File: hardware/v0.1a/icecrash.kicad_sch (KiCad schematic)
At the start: 62 parts, among them J1 SNES, J2 HDMI_A, J3 pkl_jumper, J5 Conn_02x08_Odd_Even, SW1 TACT, U1 74LVC2T45, U2 74LVC2T45, U3 74LVC2T45, U4 SII902xA-mod, U5 TLV62568DBV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

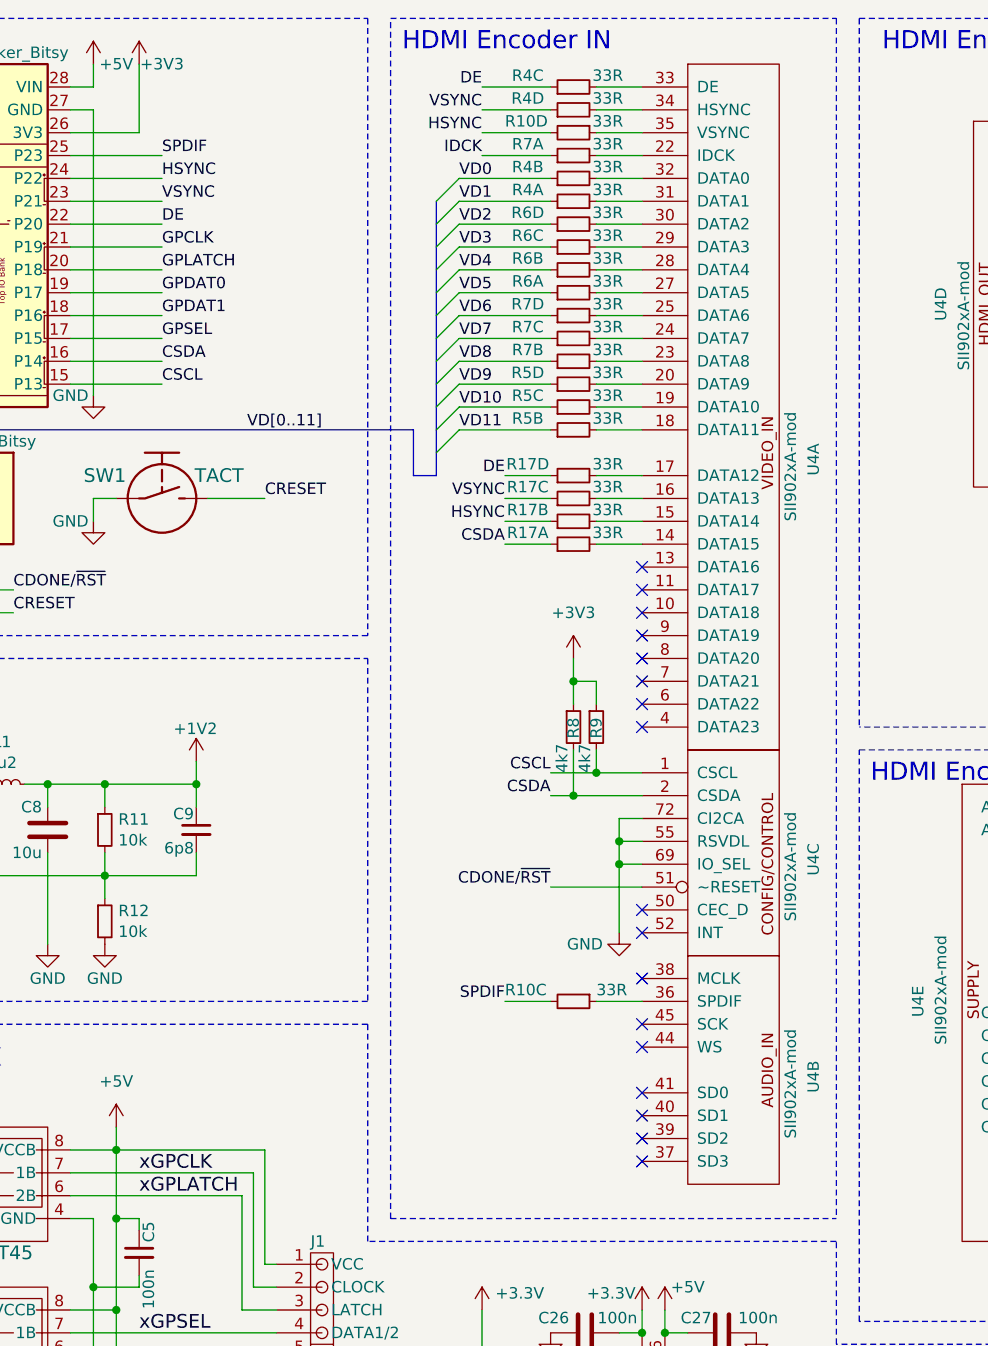
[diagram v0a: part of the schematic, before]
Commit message: Changed the HDMI encoder wiring a bit.
It is better to leave the sync signals alone. We can double assign some
of the data pins to gain access to a bunch of additional video data
modes. Now `d[7:4]` are also connected to `d[15:12]`.
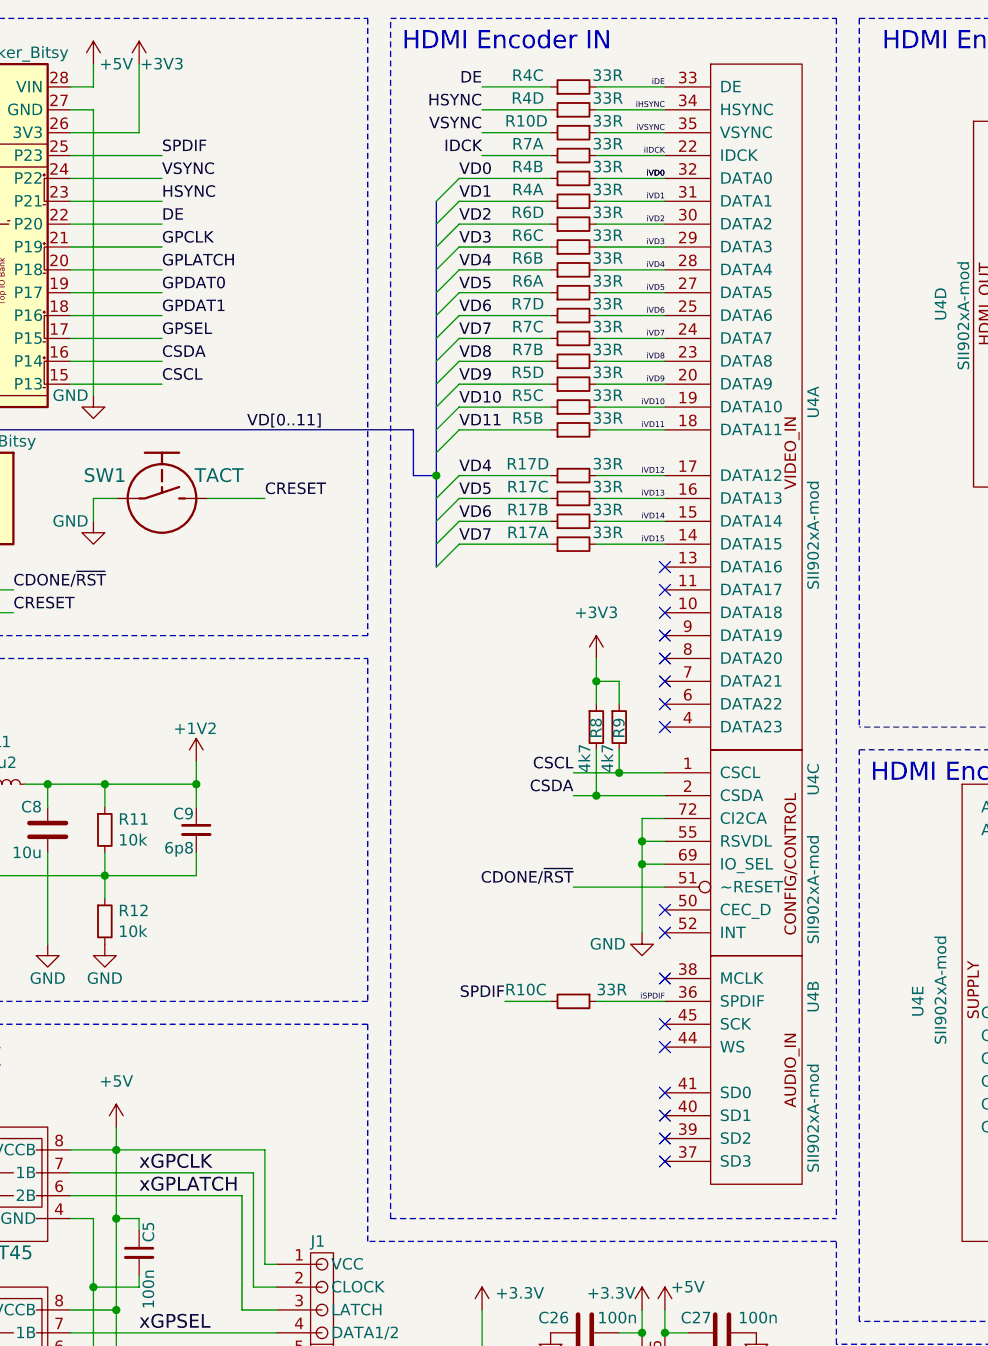
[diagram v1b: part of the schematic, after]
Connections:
- net CSDA: no longer R17.1
- net DE: no longer R17.7
- net HSYNC: now also A1.23 (P21), R4.7; no longer A1.24 (P22), R10.8, R17.3
- net VD4: now also R17.7
- net VD5: now also R17.5
- net VD6: now also R17.3
- net VD7: now also R17.1
- net VSYNC: now also A1.24 (P22), R10.8; no longer A1.23 (P21), R17.5, R4.7
- net iSPDIF: now reaches R10.5, U4.36 (SPDIF)
- net iVD5: now reaches R6.2, U4.27 (DATA5)
- net iVD13: now reaches R17.6, U4.16 (DATA13)
- net iVD0: now reaches R4.4, U4.32 (DATA0)
- net iVSYNC: now reaches R10.7, U4.35 (VSYNC)
- net iVD4: now reaches R6.4, U4.28 (DATA4)
- net iVD14: now reaches R17.4, U4.15 (DATA14)
- net iVD3: now reaches R6.6, U4.29 (DATA3)
- net iDE: now reaches R4.6, U4.33 (DE)
- net iVD6: now reaches R7.8, U4.25 (DATA6)
- net iVD10: now reaches R5.6, U4.19 (DATA10)
- net iVD8: now reaches R7.4, U4.23 (DATA8)
- net iIDCK: now reaches R7.2, U4.22 (IDCK)
- net iVD2: now reaches R6.8, U4.30 (DATA2)
- net iVD11: now reaches R5.4, U4.18 (DATA11)
- net iHSYNC: now reaches R4.8, U4.34 (HSYNC)
- net iVD12: now reaches R17.8, U4.17 (DATA12)
- net iVD7: now reaches R7.6, U4.24 (DATA7)
- net iVD1: now reaches R4.2, U4.31 (DATA1)
- net iVD15: now reaches R17.2, U4.14 (DATA15)
- net iVD9: now reaches R5.8, U4.20 (DATA9)
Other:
- moved on the sheet: R8, R9, U4A, U4B, U4C

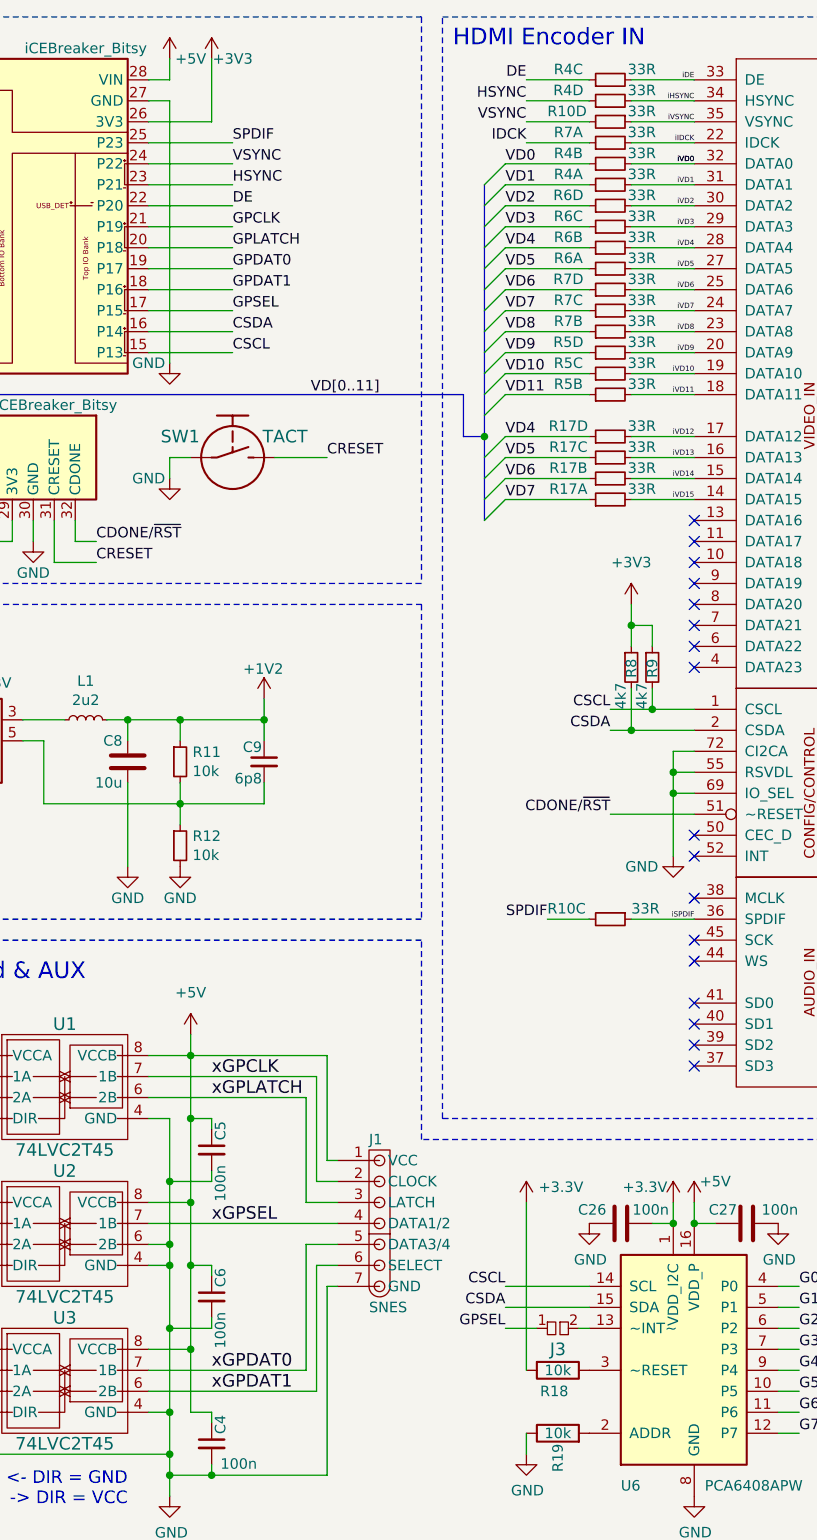
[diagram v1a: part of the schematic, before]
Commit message: More compression work. Fixed a few bugs, added silkscreen.
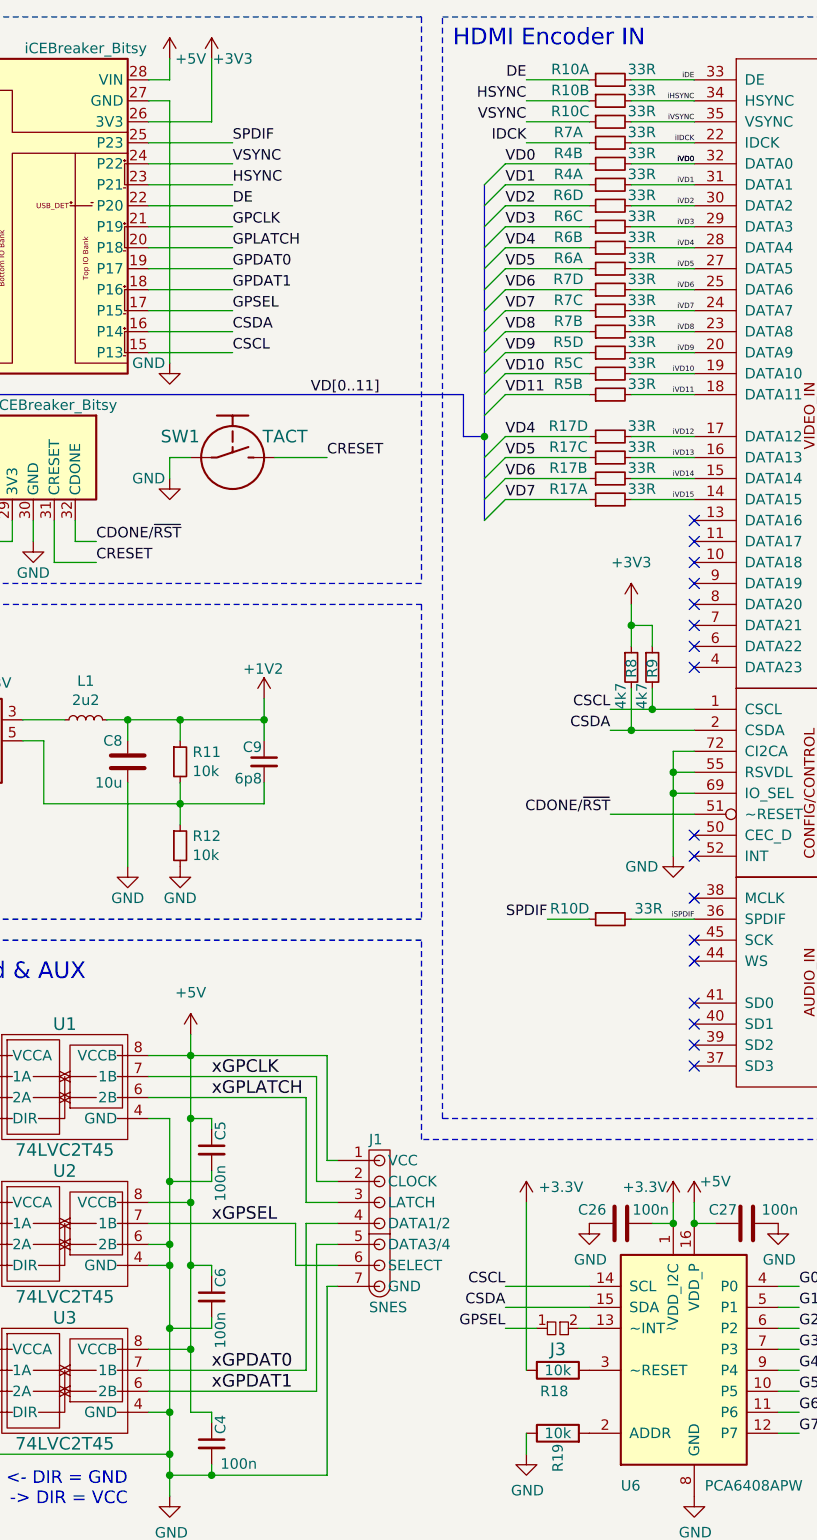
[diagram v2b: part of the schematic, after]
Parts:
- removed unit 3 of R4
- removed unit 4 of R4
- added unit 2 of R10
- added unit 1 of R10
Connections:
- net DE: now also R10.1
- net HSYNC: now also R10.3
- net SPDIF: now also R10.7; no longer R10.6
- net VSYNC: now also R10.5; no longer R10.8
- net iDE: now also R10.2
- net iHSYNC: now also R10.4
- net iSPDIF: now also R10.8; no longer R10.5
- net iVSYNC: now also R10.6; no longer R10.7
- net xGPDAT0: now also J1.4 (DATA1/2); no longer J1.5 (DATA3/4)
- net xGPDAT1: now also J1.5 (DATA3/4); no longer J1.6 (SELECT)
- net xGPSEL: now also J1.6 (SELECT); no longer J1.4 (DATA1/2)
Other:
- moved on the sheet: R10C, R10D
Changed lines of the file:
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@@
     (stroke (width 0) (type solid) (color 0 0 0 0))
   )
-  (wire (pts (xy 55.88 158.75) (xy 78.74 158.75))
+  (wire (pts (xy 55.88 158.75) (xy 73.66 158.75))
     (stroke (width 0) (type solid) (color 0 0 0 0))
   )
@@
     (stroke (width 0) (type solid) (color 0 0 0 0))
   )
+  (wire (pts (xy 73.66 158.75) (xy 73.66 163.83))
+    (stroke (width 0) (type solid) (color 0 0 0 0))
+  )
+  (wire (pts (xy 73.66 163.83) (xy 78.74 163.83))
+    (stroke (width 0) (type solid) (color 0 0 0 0))
+  )
   (wire (pts (xy 74.93 156.21) (xy 74.93 143.51))
     (stroke (width 0) (type solid) (color 0 0 0 0))
@@
     (stroke (width 0) (type solid) (color 0 0 0 0))
   )
-  (wire (pts (xy 74.93 161.29) (xy 74.93 176.53))
+  (wire (pts (xy 74.93 158.75) (xy 74.93 176.53))
     (stroke (width 0) (type solid) (color 0 0 0 0))
   )
-  (wire (pts (xy 74.93 161.29) (xy 78.74 161.29))
+  (wire (pts (xy 74.93 158.75) (xy 78.74 158.75))
     (stroke (width 0) (type solid) (color 0 0 0 0))
   )
@@
     (stroke (width 0) (type solid) (color 0 0 0 0))
   )
-  (wire (pts (xy 76.2 163.83) (xy 76.2 179.07))
+  (wire (pts (xy 76.2 161.29) (xy 76.2 179.07))
     (stroke (width 0) (type solid) (color 0 0 0 0))
   )
-  (wire (pts (xy 76.2 163.83) (xy 78.74 163.83))
+  (wire (pts (xy 76.2 161.29) (xy 78.74 161.29))
     (stroke (width 0) (type solid) (color 0 0 0 0))
   )
@@
     (pin "2")
   )
-  (symbol (lib_id "pkl_device:pkl_R4_Small") (at 111.76 20.32 90) (unit 3)
+  (symbol (lib_id "pkl_device:pkl_R4_Small") (at 111.76 20.32 90) (mirror x) (unit 1)
     (in_bom yes) (on_board yes)
-    (property "Reference" "R4" (id 0) (at 106.68 19.05 90))
-    (property "Value" "33R" (id 1) (at 115.57 19.05 90))
-    (property "Footprint" "pkl_dipol:R_Array_Convex_4x0402" (id 2) (at 111.76 17.78 90)
+    (property "Reference" "R10" (id 0) (at 109.2199 19.05 90)
+      (effects (font (size 1.27 1.27)) (justify left))
+    )
+    (property "Value" "33R" (id 1) (at 115.5699 19.05 90))
+    (property "Footprint" "pkl_dipol:R_Array_Convex_4x0402" (id 2) (at 111.76 20.32 0)
       (effects (font (size 1.524 1.524)) hide)
     )
@@
       (effects (font (size 1.524 1.524)) hide)
     )
-    (property "1b2-key" "res-0402x4-33r" (id 4) (at 111.76 20.32 0)
-      (effects (font (size 1.27 1.27)) hide)
-    )
-    (pin "5")
-    (pin "6")
+    (pin "1")
+    (pin "2")
   )
-  (symbol (lib_id "pkl_device:pkl_R4_Small") (at 111.76 22.86 90) (unit 4)
+  (symbol (lib_id "pkl_device:pkl_R4_Small") (at 111.76 22.86 90) (mirror x) (unit 2)
     (in_bom yes) (on_board yes)
-    (property "Reference" "R4" (id 0) (at 106.68 21.59 90))
-    (property "Value" "33R" (id 1) (at 115.57 21.59 90))
-    (property "Footprint" "pkl_dipol:R_Array_Convex_4x0402" (id 2) (at 111.76 20.32 90)
+    (property "Reference" "R10" (id 0) (at 109.2199 21.59 90)
+      (effects (font (size 1.27 1.27)) (justify left))
+    )
+    (property "Value" "33R" (id 1) (at 115.5699 21.59 90))
+    (property "Footprint" "pkl_dipol:R_Array_Convex_4x0402" (id 2) (at 111.76 22.86 0)
       (effects (font (size 1.524 1.524)) hide)
     )
@@
       (effects (font (size 1.524 1.524)) hide)
     )
-    (property "1b2-key" "res-0402x4-33r" (id 4) (at 111.76 22.86 0)
-      (effects (font (size 1.27 1.27)) hide)
-    )
-    (pin "7")
-    (pin "8")
+    (pin "3")
+    (pin "4")
   )
-  (symbol (lib_id "pkl_device:pkl_R4_Small") (at 111.76 25.4 270) (unit 4)
+  (symbol (lib_id "pkl_device:pkl_R4_Small") (at 111.76 25.4 90) (mirror x) (unit 3)
     (in_bom yes) (on_board yes)
-    (property "Reference" "R10" (id 0) (at 104.1401 24.13 90)
+    (property "Reference" "R10" (id 0) (at 109.2199 24.13 90)
       (effects (font (size 1.27 1.27)) (justify left))
     )
-    (property "Value" "33R" (id 1) (at 115.5701 24.13 90))
+    (property "Value" "33R" (id 1) (at 115.5699 24.13 90))
     (property "Footprint" "pkl_dipol:R_Array_Convex_4x0402" (id 2) (at 111.76 25.4 0)
       (effects (font (size 1.524 1.524)) hide)
@@
       (effects (font (size 1.524 1.524)) hide)
     )
-    (pin "7")
-    (pin "8")
+    (pin "5")
+    (pin "6")
   )
   (symbol (lib_id "pkl_device:pkl_R4_Small") (at 111.76 27.94 90) (unit 1)
@@
     (pin "2")
   )
-  (symbol (lib_id "pkl_device:pkl_R4_Small") (at 111.76 121.92 270) (unit 3)
+  (symbol (lib_id "pkl_device:pkl_R4_Small") (at 111.76 121.92 90) (mirror x) (unit 4)
     (in_bom yes) (on_board yes)
-    (property "Reference" "R10" (id 0) (at 104.1401 120.65 90)
+    (property "Reference" "R10" (id 0) (at 109.2199 120.65 90)
       (effects (font (size 1.27 1.27)) (justify left))
     )
-    (property "Value" "33R" (id 1) (at 114.3001 120.65 90)
+    (property "Value" "33R" (id 1) (at 118.1099 120.65 90)
       (effects (font (size 1.27 1.27)) (justify left))
     )
@@
       (effects (font (size 1.524 1.524)) hide)
     )
-    (pin "5")
-    (pin "6")
+    (pin "7")
+    (pin "8")
   )
   (symbol (lib_id "pkl_device:pkl_R_Small") (at 114.3 91.44 0) (unit 1)
@@
       (reference "R4") (unit 2) (value "33R") (footprint "pkl_dipol:R_Array_Convex_4x0402")
     )
-    (path "/406c086f-5cc7-46a7-9af2-5ae15f38df90"
-      (reference "R4") (unit 3) (value "33R") (footprint "pkl_dipol:R_Array_Convex_4x0402")
-    )
-    (path "/7f4ab92d-696f-4aee-bc16-637296bbac60"
-      (reference "R4") (unit 4) (value "33R") (footprint "pkl_dipol:R_Array_Convex_4x0402")
-    )
     (path "/7eea41ec-4f0b-499b-afe1-8cd83116c438"
       (reference "R5") (unit 2) (value "33R") (footprint "pkl_dipol:R_Array_Convex_4x0402")
@@
       (reference "R9") (unit 1) (value "4k7") (footprint "pkl_dipol:R_0402")
     )
-    (path "/04658c8f-49be-4281-98d0-0e4a5fff71a4"
-      (reference "R10") (unit 3) (value "33R") (footprint "pkl_dipol:R_Array_Convex_4x0402")
+    (path "/fa593727-e05b-48dc-b4a1-78a82fc857bd"
+      (reference "R10") (unit 1) (value "33R") (footprint "pkl_dipol:R_Array_Convex_4x0402")
+    )
+    (path "/27b8a318-3b1a-4c2b-aca2-6c12967f13f6"
+      (reference "R10") (unit 2) (value "33R") (footprint "pkl_dipol:R_Array_Convex_4x0402")
     )
     (path "/1edb5f16-4d0c-453b-a9ed-8c75c81b5939"
+      (reference "R10") (unit 3) (value "33R") (footprint "pkl_dipol:R_Array_Convex_4x0402")
+    )
+    (path "/04658c8f-49be-4281-98d0-0e4a5fff71a4"
       (reference "R10") (unit 4) (value "33R") (footprint "pkl_dipol:R_Array_Convex_4x0402")
     )
